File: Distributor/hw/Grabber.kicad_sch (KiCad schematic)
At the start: 16 parts, among them J7 Conn_01x04, J8 Conn_01x06_MountingPin, J9 Conn_02x09_Odd_Even, U7 STM32G070CBTx, U8 MLX90640ESF-BAB-000-TU

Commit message: Revise distributor board; submit for fab
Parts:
- renumbered D3 to D7, D4 to D8, R6 to R10, R7 to R11, R8 to R12, R4 to R8, R5 to R9
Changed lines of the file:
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@@
   (symbol (lib_id "Device:R") (at 180.975 61.595 0) (unit 1)
     (in_bom yes) (on_board yes) (dnp no)
-    (property "Reference" "R8" (at 182.88 60.325 0)
+    (property "Reference" "R12" (at 182.88 60.325 0)
       (effects (font (size 1.27 1.27)) (justify left))
     )
@@
       (project "Distributor"
         (path "/3f67d80a-1b5b-4b57-a63e-46eb7de4787a/d071538b-874a-4835-97d2-570c76260972"
+          (reference "R12") (unit 1)
+        )
+      )
+    )
+  )
+  (symbol (lib_id "Device:C") (at 71.12 142.875 0) (unit 1)
+    (in_bom yes) (on_board yes) (dnp no)
+    (property "Reference" "C16" (at 74.295 141.605 0)
+      (effects (font (size 1.27 1.27)) (justify left))
+    )
+    (property "Value" "100n" (at 74.295 144.145 0)
+      (effects (font (size 1.27 1.27)) (justify left))
+    )
+    (property "Footprint" "Capacitor_SMD:C_0603_1608Metric" (at 72.0852 146.685 0)
+      (effects (font (size 1.27 1.27)) hide)
+    )
+    (property "Datasheet" "~" (at 71.12 142.875 0)
+      (effects (font (size 1.27 1.27)) hide)
+    )
+    (pin "1")
+    (pin "2")
+    (instances
+      (project "Distributor"
+        (path "/3f67d80a-1b5b-4b57-a63e-46eb7de4787a/d071538b-874a-4835-97d2-570c76260972"
+          (reference "C16") (unit 1)
+        )
+      )
+    )
+  )
+  (symbol (lib_id "power:GND") (at 149.225 81.28 0) (unit 1)
+    (in_bom yes) (on_board yes) (dnp no) (fields_autoplaced)
+    (property "Reference" "#PWR053" (at 149.225 87.63 0)
+      (effects (font (size 1.27 1.27)) hide)
+    )
+    (property "Value" "GND" (at 149.225 85.725 0)
+      (effects (font (size 1.27 1.27)) hide)
+    )
+    (property "Footprint" "" (at 149.225 81.28 0)
+      (effects (font (size 1.27 1.27)) hide)
+    )
+    (property "Datasheet" "" (at 149.225 81.28 0)
+      (effects (font (size 1.27 1.27)) hide)
+    )
+    (pin "1")
+    (instances
+      (project "Distributor"
+        (path "/3f67d80a-1b5b-4b57-a63e-46eb7de4787a/d071538b-874a-4835-97d2-570c76260972"
+          (reference "#PWR053") (unit 1)
+        )
+      )
+    )
+  )
+  (symbol (lib_id "power:GND") (at 41.275 62.23 0) (unit 1)
+    (in_bom yes) (on_board yes) (dnp no) (fields_autoplaced)
+    (property "Reference" "#PWR047" (at 41.275 68.58 0)
+      (effects (font (size 1.27 1.27)) hide)
+    )
+    (property "Value" "GND" (at 41.275 66.675 0)
+      (effects (font (size 1.27 1.27)) hide)
+    )
+    (property "Footprint" "" (at 41.275 62.23 0)
+      (effects (font (size 1.27 1.27)) hide)
+    )
+    (property "Datasheet" "" (at 41.275 62.23 0)
+      (effects (font (size 1.27 1.27)) hide)
+    )
+    (pin "1")
+    (instances
+      (project "Distributor"
+        (path "/3f67d80a-1b5b-4b57-a63e-46eb7de4787a/d071538b-874a-4835-97d2-570c76260972"
+          (reference "#PWR047") (unit 1)
+        )
+      )
+    )
+  )
+  (symbol (lib_id "Device:R") (at 149.225 77.47 0) (unit 1)
+    (in_bom yes) (on_board yes) (dnp no)
+    (property "Reference" "R8" (at 151.13 76.2 0)
+      (effects (font (size 1.27 1.27)) (justify left))
+    )
+    (property "Value" "1M" (at 151.13 78.74 0)
+      (effects (font (size 1.27 1.27)) (justify left))
+    )
+    (property "Footprint" "Resistor_SMD:R_0603_1608Metric" (at 147.447 77.47 90)
+      (effects (font (size 1.27 1.27)) hide)
+    )
+    (property "Datasheet" "~" (at 149.225 77.47 0)
+      (effects (font (size 1.27 1.27)) hide)
+    )
+    (pin "2")
+    (pin "1")
+    (instances
+      (project "Distributor"
+        (path "/3f67d80a-1b5b-4b57-a63e-46eb7de4787a/d071538b-874a-4835-97d2-570c76260972"
           (reference "R8") (unit 1)
         )
@@
     )
   )
-  (symbol (lib_id "Device:C") (at 71.12 142.875 0) (unit 1)
-    (in_bom yes) (on_board yes) (dnp no)
-    (property "Reference" "C16" (at 74.295 141.605 0)
-      (effects (font (size 1.27 1.27)) (justify left))
-    )
-    (property "Value" "100n" (at 74.295 144.145 0)
-      (effects (font (size 1.27 1.27)) (justify left))
-    )
-    (property "Footprint" "Capacitor_SMD:C_0603_1608Metric" (at 72.0852 146.685 0)
-      (effects (font (size 1.27 1.27)) hide)
-    )
-    (property "Datasheet" "~" (at 71.12 142.875 0)
-      (effects (font (size 1.27 1.27)) hide)
-    )
-    (pin "1")
-    (pin "2")
-    (instances
-      (project "Distributor"
-        (path "/3f67d80a-1b5b-4b57-a63e-46eb7de4787a/d071538b-874a-4835-97d2-570c76260972"
-          (reference "C16") (unit 1)
-        )
-      )
-    )
-  )
-  (symbol (lib_id "power:GND") (at 149.225 81.28 0) (unit 1)
-    (in_bom yes) (on_board yes) (dnp no) (fields_autoplaced)
-    (property "Reference" "#PWR053" (at 149.225 87.63 0)
-      (effects (font (size 1.27 1.27)) hide)
-    )
-    (property "Value" "GND" (at 149.225 85.725 0)
-      (effects (font (size 1.27 1.27)) hide)
-    )
-    (property "Footprint" "" (at 149.225 81.28 0)
-      (effects (font (size 1.27 1.27)) hide)
-    )
-    (property "Datasheet" "" (at 149.225 81.28 0)
-      (effects (font (size 1.27 1.27)) hide)
-    )
-    (pin "1")
-    (instances
-      (project "Distributor"
-        (path "/3f67d80a-1b5b-4b57-a63e-46eb7de4787a/d071538b-874a-4835-97d2-570c76260972"
-          (reference "#PWR053") (unit 1)
-        )
-      )
-    )
-  )
-  (symbol (lib_id "power:GND") (at 41.275 62.23 0) (unit 1)
-    (in_bom yes) (on_board yes) (dnp no) (fields_autoplaced)
-    (property "Reference" "#PWR047" (at 41.275 68.58 0)
-      (effects (font (size 1.27 1.27)) hide)
-    )
-    (property "Value" "GND" (at 41.275 66.675 0)
-      (effects (font (size 1.27 1.27)) hide)
-    )
-    (property "Footprint" "" (at 41.275 62.23 0)
-      (effects (font (size 1.27 1.27)) hide)
-    )
-    (property "Datasheet" "" (at 41.275 62.23 0)
-      (effects (font (size 1.27 1.27)) hide)
-    )
-    (pin "1")
-    (instances
-      (project "Distributor"
-        (path "/3f67d80a-1b5b-4b57-a63e-46eb7de4787a/d071538b-874a-4835-97d2-570c76260972"
-          (reference "#PWR047") (unit 1)
-        )
-      )
-    )
-  )
-  (symbol (lib_id "Device:R") (at 149.225 77.47 0) (unit 1)
-    (in_bom yes) (on_board yes) (dnp no)
-    (property "Reference" "R4" (at 151.13 76.2 0)
-      (effects (font (size 1.27 1.27)) (justify left))
-    )
-    (property "Value" "1M" (at 151.13 78.74 0)
-      (effects (font (size 1.27 1.27)) (justify left))
-    )
-    (property "Footprint" "Resistor_SMD:R_0603_1608Metric" (at 147.447 77.47 90)
-      (effects (font (size 1.27 1.27)) hide)
-    )
-    (property "Datasheet" "~" (at 149.225 77.47 0)
-      (effects (font (size 1.27 1.27)) hide)
-    )
-    (pin "2")
-    (pin "1")
-    (instances
-      (project "Distributor"
-        (path "/3f67d80a-1b5b-4b57-a63e-46eb7de4787a/d071538b-874a-4835-97d2-570c76260972"
-          (reference "R4") (unit 1)
-        )
-      )
-    )
-  )
   (symbol (lib_id "power:GND") (at 27.94 154.94 0) (unit 1)
     (in_bom yes) (on_board yes) (dnp no) (fields_autoplaced)
@@
   (symbol (lib_id "Device:R") (at 53.975 86.36 90) (unit 1)
     (in_bom yes) (on_board yes) (dnp no)
-    (property "Reference" "R6" (at 53.975 80.645 90)
+    (property "Reference" "R10" (at 53.975 80.645 90)
       (effects (font (size 1.27 1.27)))
     )
@@
       (project "Distributor"
         (path "/3f67d80a-1b5b-4b57-a63e-46eb7de4787a/d071538b-874a-4835-97d2-570c76260972"
-          (reference "R6") (unit 1)
+          (reference "R10") (unit 1)
         )
       )
@@
   )
   (symbol (lib_id "Device:R") (at 172.72 61.595 0) (unit 1)
-    (in_bom yes) (on_board yes) (dnp no) (fields_autoplaced)
-    (property "Reference" "R7" (at 174.625 60.325 0)
+    (in_bom yes) (on_board yes) (dnp no)
+    (property "Reference" "R11" (at 174.625 60.325 0)
       (effects (font (size 1.27 1.27)) (justify left))
     )
@@
       (project "Distributor"
         (path "/3f67d80a-1b5b-4b57-a63e-46eb7de4787a/d071538b-874a-4835-97d2-570c76260972"
-          (reference "R7") (unit 1)
+          (reference "R11") (unit 1)
         )
       )
@@
   (symbol (lib_id "Device:LED") (at 43.18 76.2 180) (unit 1)
     (in_bom yes) (on_board yes) (dnp no)
-    (property "Reference" "D3" (at 44.45 69.85 0)
+    (property "Reference" "D7" (at 44.45 69.85 0)
       (effects (font (size 1.27 1.27)))
     )
@@
       (project "Distributor"
         (path "/3f67d80a-1b5b-4b57-a63e-46eb7de4787a/d071538b-874a-4835-97d2-570c76260972"
-          (reference "D3") (unit 1)
+          (reference "D7") (unit 1)
         )
       )
@@
   (symbol (lib_id "Device:R") (at 53.975 76.2 90) (unit 1)
     (in_bom yes) (on_board yes) (dnp no)
-    (property "Reference" "R5" (at 53.975 70.485 90)
+    (property "Reference" "R9" (at 53.975 70.485 90)
       (effects (font (size 1.27 1.27)))
     )
@@
       (project "Distributor"
         (path "/3f67d80a-1b5b-4b57-a63e-46eb7de4787a/d071538b-874a-4835-97d2-570c76260972"
-          (reference "R5") (unit 1)
+          (reference "R9") (unit 1)
         )
       )
@@
   (symbol (lib_id "Device:LED") (at 43.18 86.36 180) (unit 1)
     (in_bom yes) (on_board yes) (dnp no)
-    (property "Reference" "D4" (at 44.45 80.01 0)
+    (property "Reference" "D8" (at 44.45 80.01 0)
       (effects (font (size 1.27 1.27)))
     )
@@
       (project "Distributor"
         (path "/3f67d80a-1b5b-4b57-a63e-46eb7de4787a/d071538b-874a-4835-97d2-570c76260972"
-          (reference "D4") (unit 1)
-        )
-      )
+          (reference "D8") (unit 1)
+        )
+      )

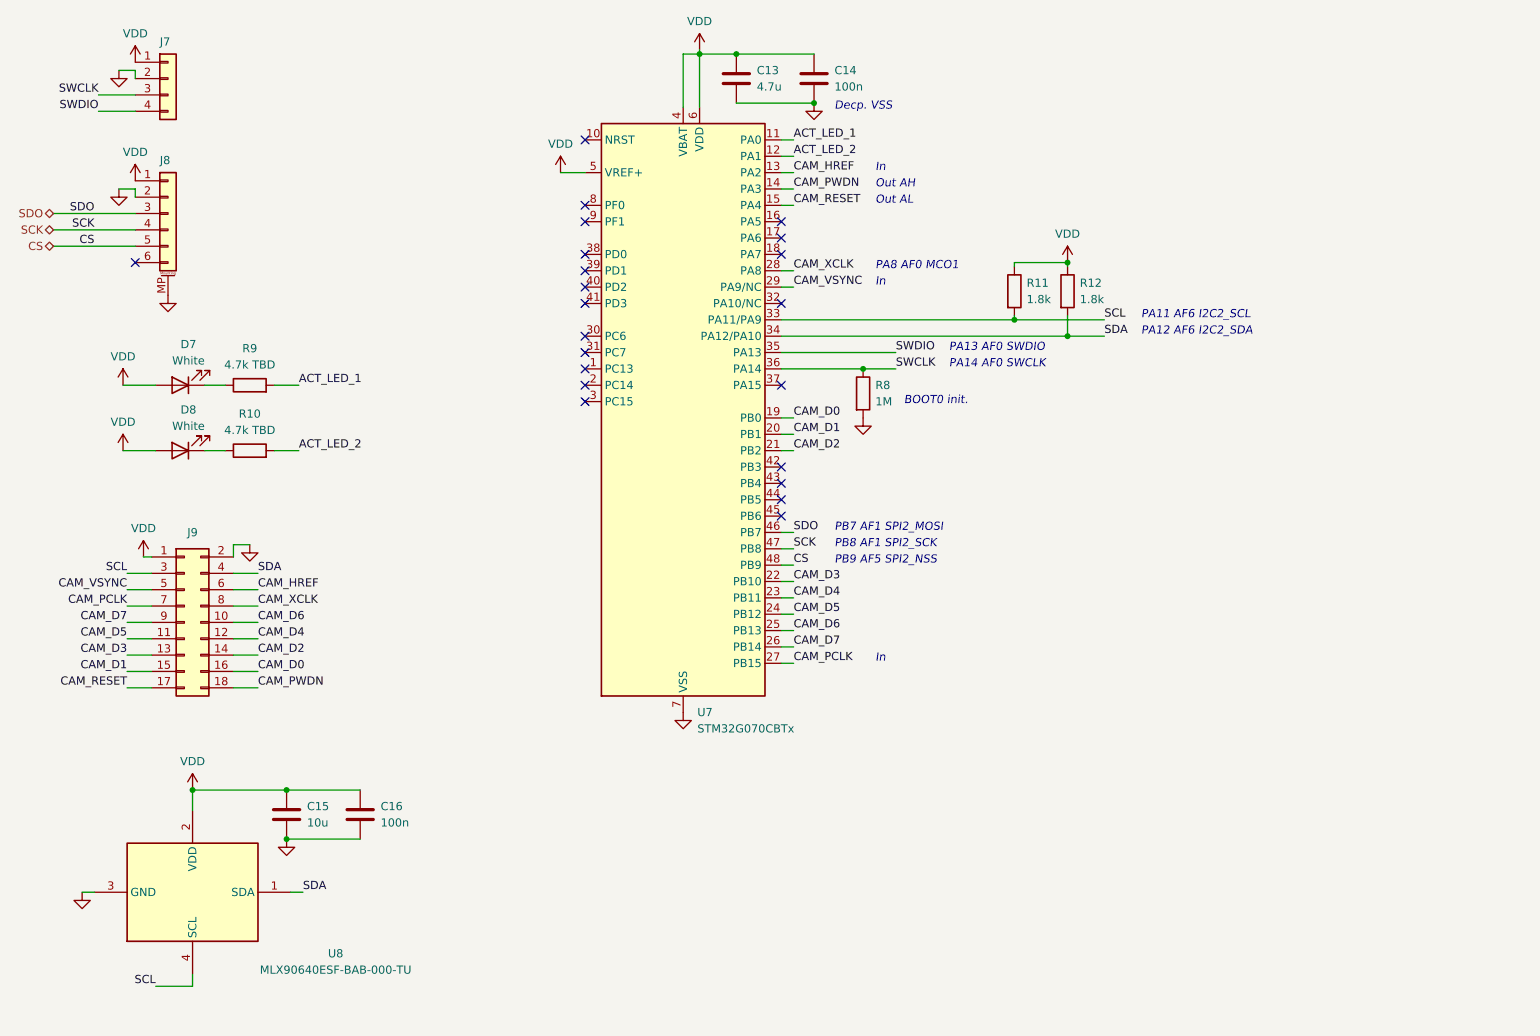
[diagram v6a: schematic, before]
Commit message: Revise schematic, replacing camera unit MCU with STM32F407Vxxx
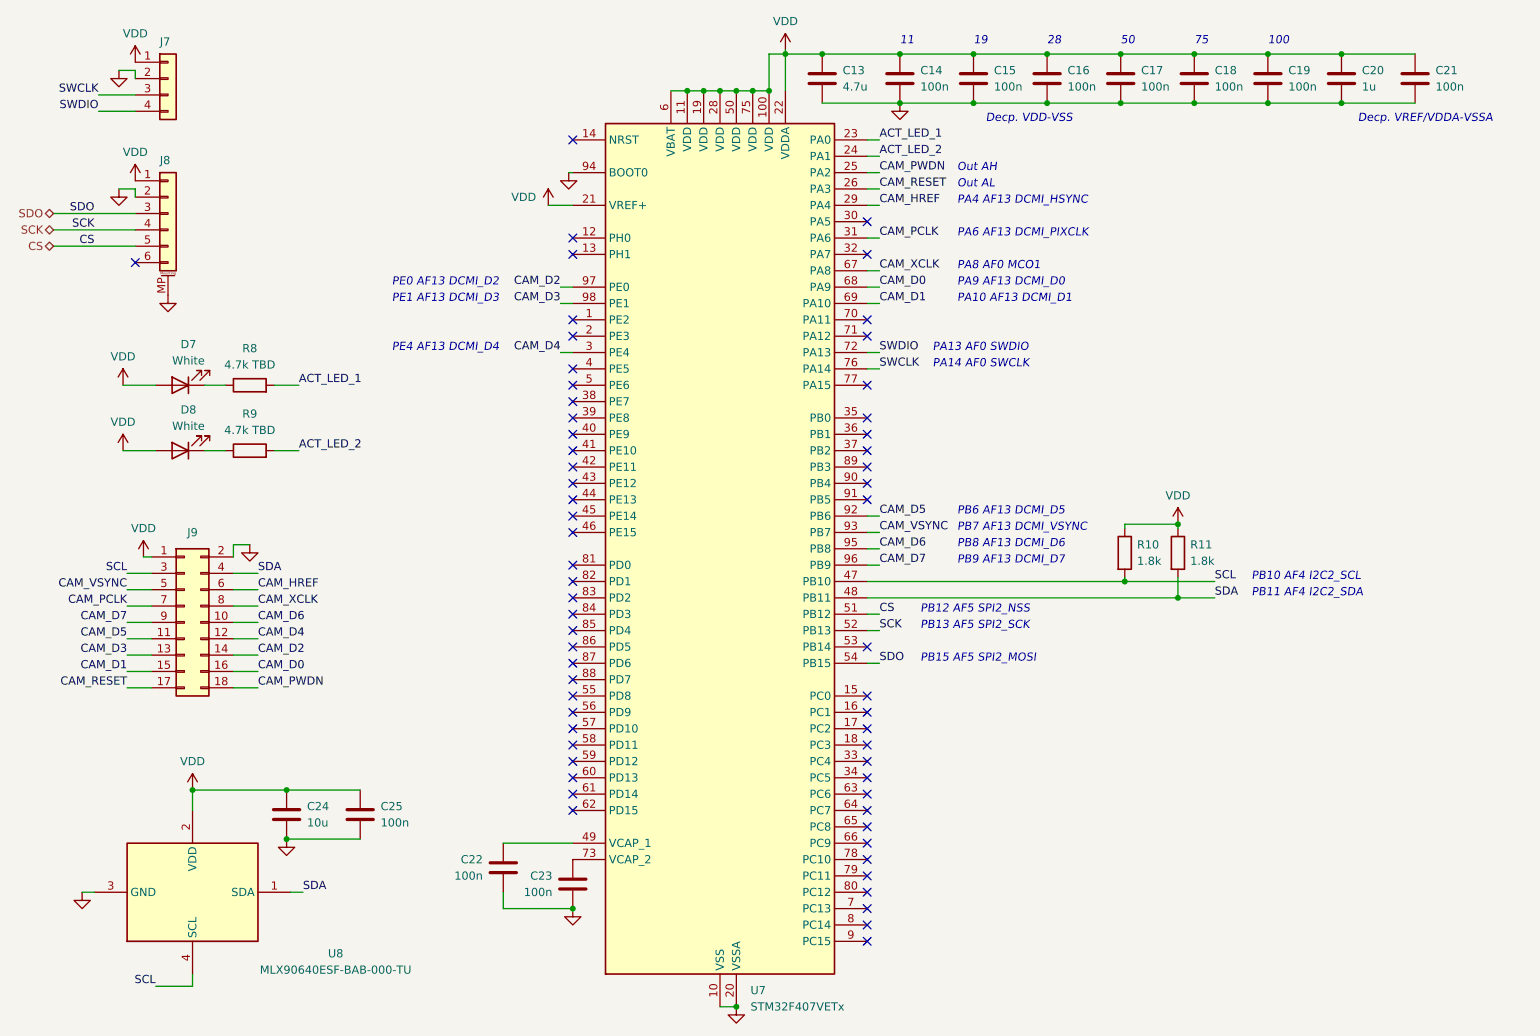
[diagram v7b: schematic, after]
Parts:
- removed R8: 1M, Resistor_SMD:R_0603_1608Metric, symbol Device:R
- removed U7: STM32G070CBTx, Package_QFP:LQFP-48_7x7mm_P0.5mm, symbol MCU_ST_STM32G0:STM32G070CBTx
- added C15, C16, C17, C18, C19, C21, C22, C23: 100n, Capacitor_SMD:C_0603_1608Metric, symbol Device:C
- added C20: 1u, Capacitor_SMD:C_0603_1608Metric, symbol Device:C
- added U7: STM32F407VETx, Package_QFP:LQFP-100_14x14mm_P0.5mm, symbol MCU_ST_STM32F4:STM32F407VETx
- renumbered C15 to C24, C16 to C25, R11 to R10, R12 to R11, R9 to R8, R10 to R9
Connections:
- net ACT_LED_1: now also U7.23 (PA0)
- net ACT_LED_2: now also U7.24 (PA1)
- net CAM_D0: now also U7.68 (PA9)
- net CAM_D1: now also U7.69 (PA10)
- net CAM_D2: now also U7.97 (PE0)
- net CAM_D3: now also U7.98 (PE1)
- net CAM_D4: now also U7.3 (PE4)
- net CAM_D5: now also U7.92 (PB6)
- net CAM_D6: now also U7.95 (PB8)
- net CAM_D7: now also U7.96 (PB9)
- net CAM_HREF: now also U7.29 (PA4)
- net CAM_PCLK: now also U7.31 (PA6)
- net CAM_PWDN: now also U7.25 (PA2)
- net CAM_RESET: now also U7.26 (PA3)
- net CAM_VSYNC: now also U7.93 (PB7)
- net CAM_XCLK: now also U7.67 (PA8)
- net CS: now also U7.51 (PB12)
- net GND: now also C15.2, C16.2, C17.2, C18.2, C19.2, C20.2, C21.2, C22.2, C23.2, U7.10 (VSS), U7.20 (VSSA), U7.27 (VSS), U7.74 (VSS), U7.94 (BOOT0), U7.99 (VSS)
- net SCK: now also U7.52 (PB13)
- net SCL: now also U7.47 (PB10)
- net SDA: now also U7.48 (PB11)
- net SDO: now also U7.54 (PB15)
- net SWCLK: now also U7.76 (PA14)
- net SWDIO: now also U7.72 (PA13)
- net VDD: now also C15.1, C16.1, C17.1, C18.1, C19.1, C20.1, C21.1, U7.100 (VDD), U7.11 (VDD), U7.19 (VDD), U7.21 (VREF+), U7.22 (VDDA), U7.28 (VDD), U7.50 (VDD), U7.6 (VBAT), U7.75 (VDD)
- new net: C22.1, U7.49 (VCAP_1)
- new net: C23.1, U7.73 (VCAP_2)
- no-connect marks 22 -> 61
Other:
- note added: "100"
- note added: "11"
- note added: "19"
- note added: "28"
- note added: "50"
- note added: "75"
- note added: "Decp. VDD-VSS"
- note added: "Decp. VREF/VDDA-VSSA"
- note added: "PA10 AF13 DCMI_D1"
- note added: "PA4 AF13 DCMI_HSYNC"
- note added: "PA6 AF13 DCMI_PIXCLK"
- note added: "PA9 AF13 DCMI_D0"
- note added: "PB10 AF4 I2C2_SCL"
- note added: "PB11 AF4 I2C2_SDA"
- note added: "PB12 AF5 SPI2_NSS"
- note added: "PB13 AF5 SPI2_SCK"
- note added: "PB15 AF5 SPI2_MOSI"
- note added: "PB6 AF13 DCMI_D5"
- note added: "PB7 AF13 DCMI_VSYNC"
- note added: "PB8 AF13 DCMI_D6"
- note added: "PB9 AF13 DCMI_D7"
- note added: "PE0 AF13 DCMI_D2"
- note added: "PE1 AF13 DCMI_D3"
- note added: "PE4 AF13 DCMI_D4"
- note removed: "BOOT0 init."
- note removed: "Decp. VSS"
- note removed: "In"
- note removed: "PA11 AF6 I2C2_SCL"
- note removed: "PA12 AF6 I2C2_SDA"
- note removed: "PB7 AF1 SPI2_MOSI"
- note removed: "PB8 AF1 SPI2_SCK"
- note removed: "PB9 AF5 SPI2_NSS"
- moved on the sheet: C13, C14, R10, R11
